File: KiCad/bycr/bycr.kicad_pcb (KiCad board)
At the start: 2 copper layers, 160.7 x 101.6 mm, 29 parts, among them J1 Conn_01x03, J2 Conn_01x03, J3 Conn_01x03, J4 Conn_01x03, J5 Conn_01x02, J6 Conn_01x02, SW1 SW_Push, U1 74HC595, U2 74HC595, U3 74HC165

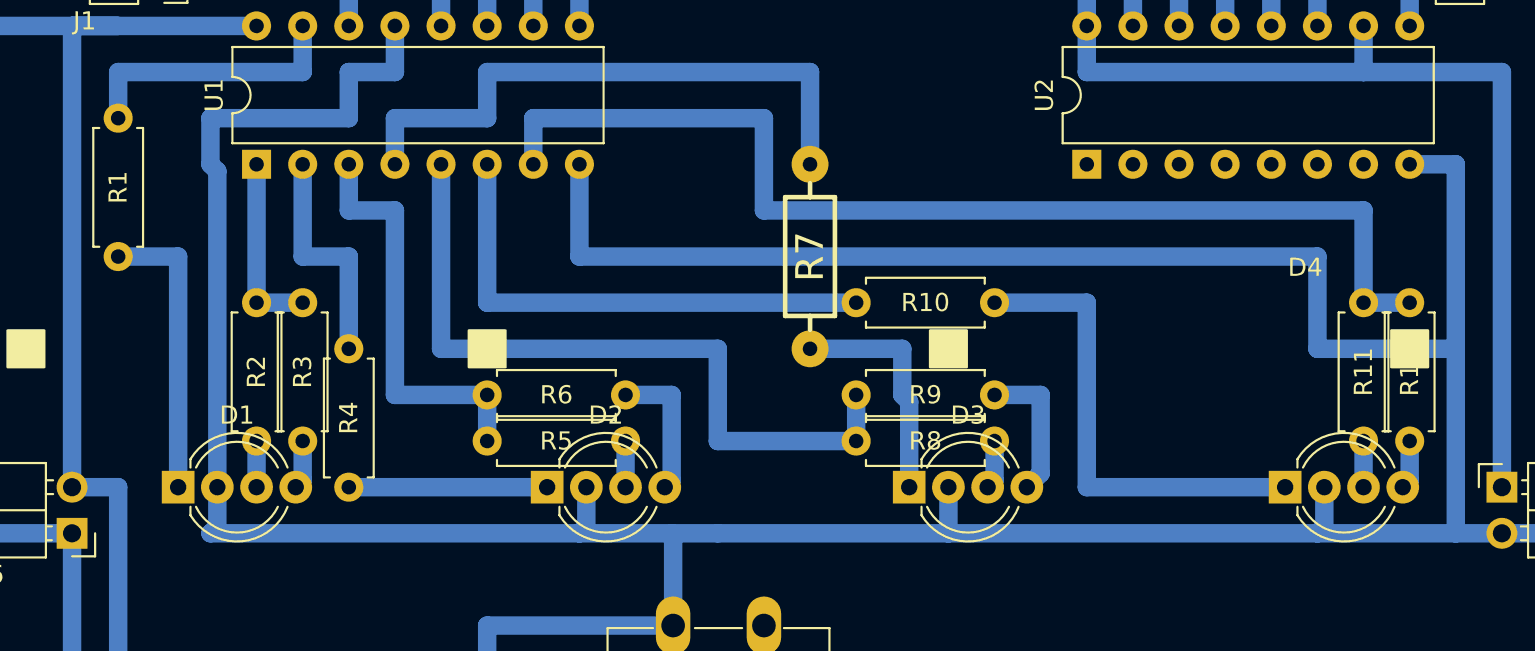
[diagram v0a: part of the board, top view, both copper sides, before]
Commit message: added custom rgbled footprint
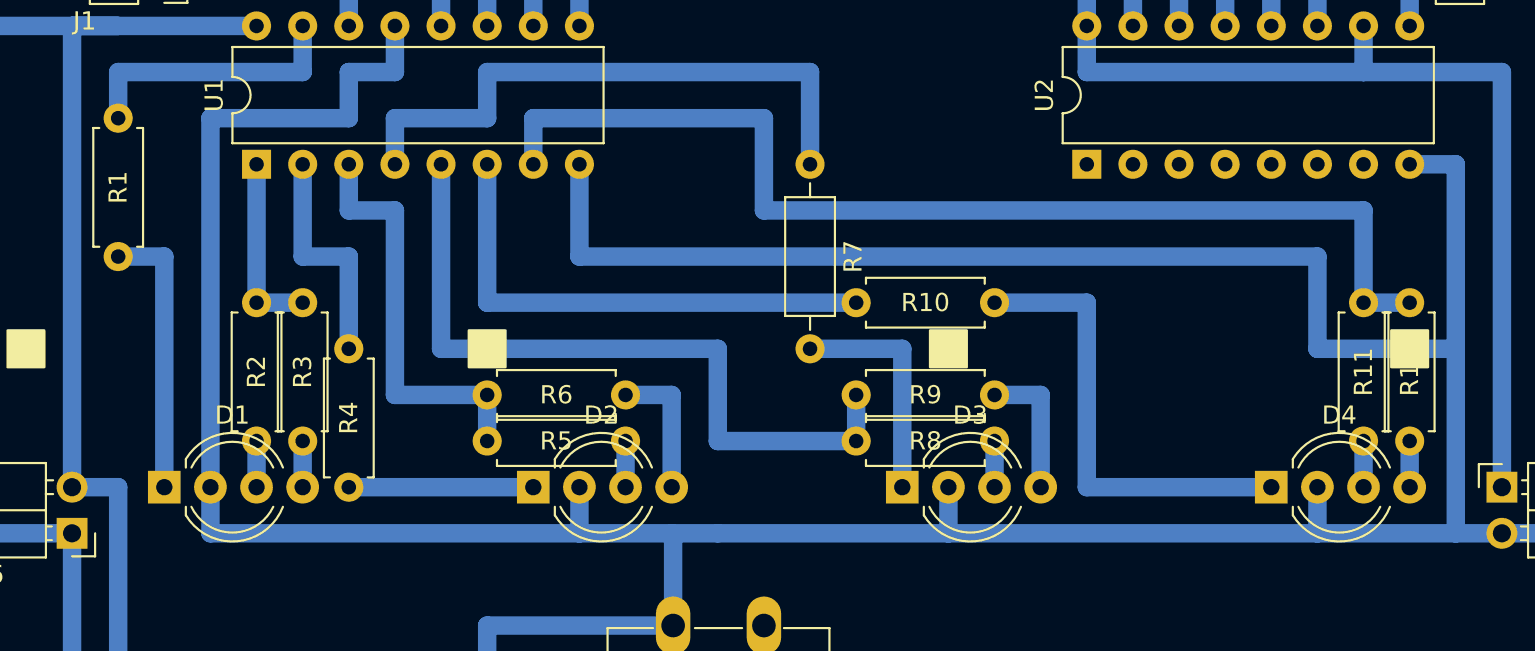
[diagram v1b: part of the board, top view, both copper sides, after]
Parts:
- D1, D2, D3, D4: footprint LED_THT:LED_D5.0mm-4_RGB_Wide_Pins -> Custom:LED_D5.0mm-4_RGB_Wide_Pins_Custom
- R7: footprint New_Library:Resistor -> Resistor_THT:R_Axial_DIN0207_L6.3mm_D2.5mm_P10.16mm_Horizontal
- moved D1 0.25 mm to (94.5, 81.3)
- moved D2 0.25 mm to (114.8, 81.3)
- moved D4 0.25 mm to (155.4, 81.3)
- moved D3 0.13 mm to (135.1, 81.3)
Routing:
- net Net-(D4-RA): track 26.2 -> 25.4 mm
- net Net-(D2-RA): track 10.9 -> 10.2 mm
- net Net-(D1-RA): track 16.0 -> 15.2 mm
- net GNDREF: track 458.3 -> 457.7 mm

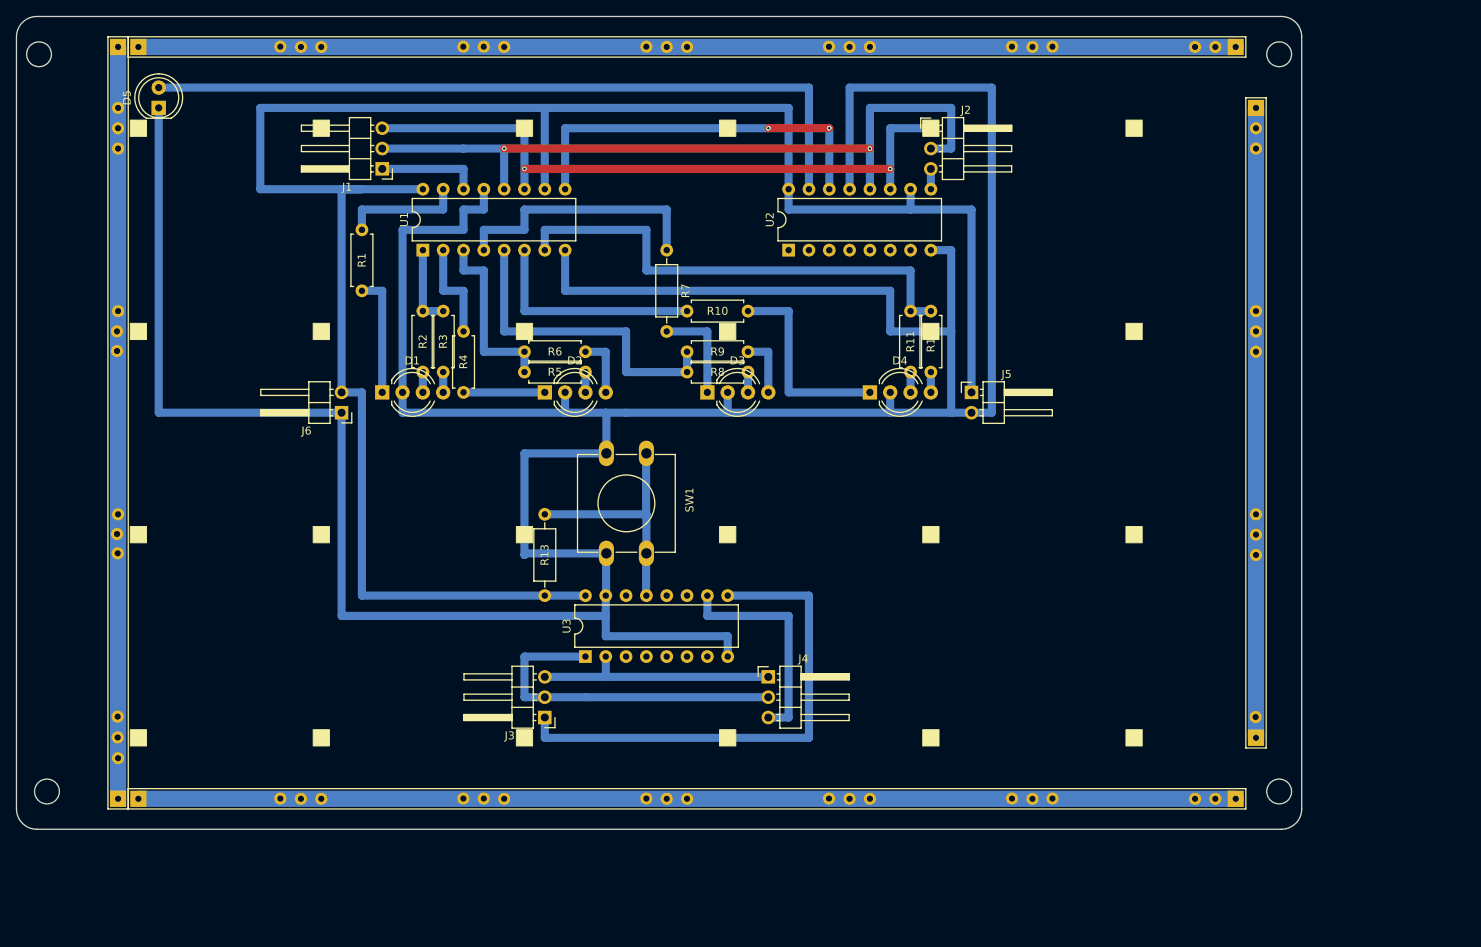
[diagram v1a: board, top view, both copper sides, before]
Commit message: rename bycr to bycr_hand
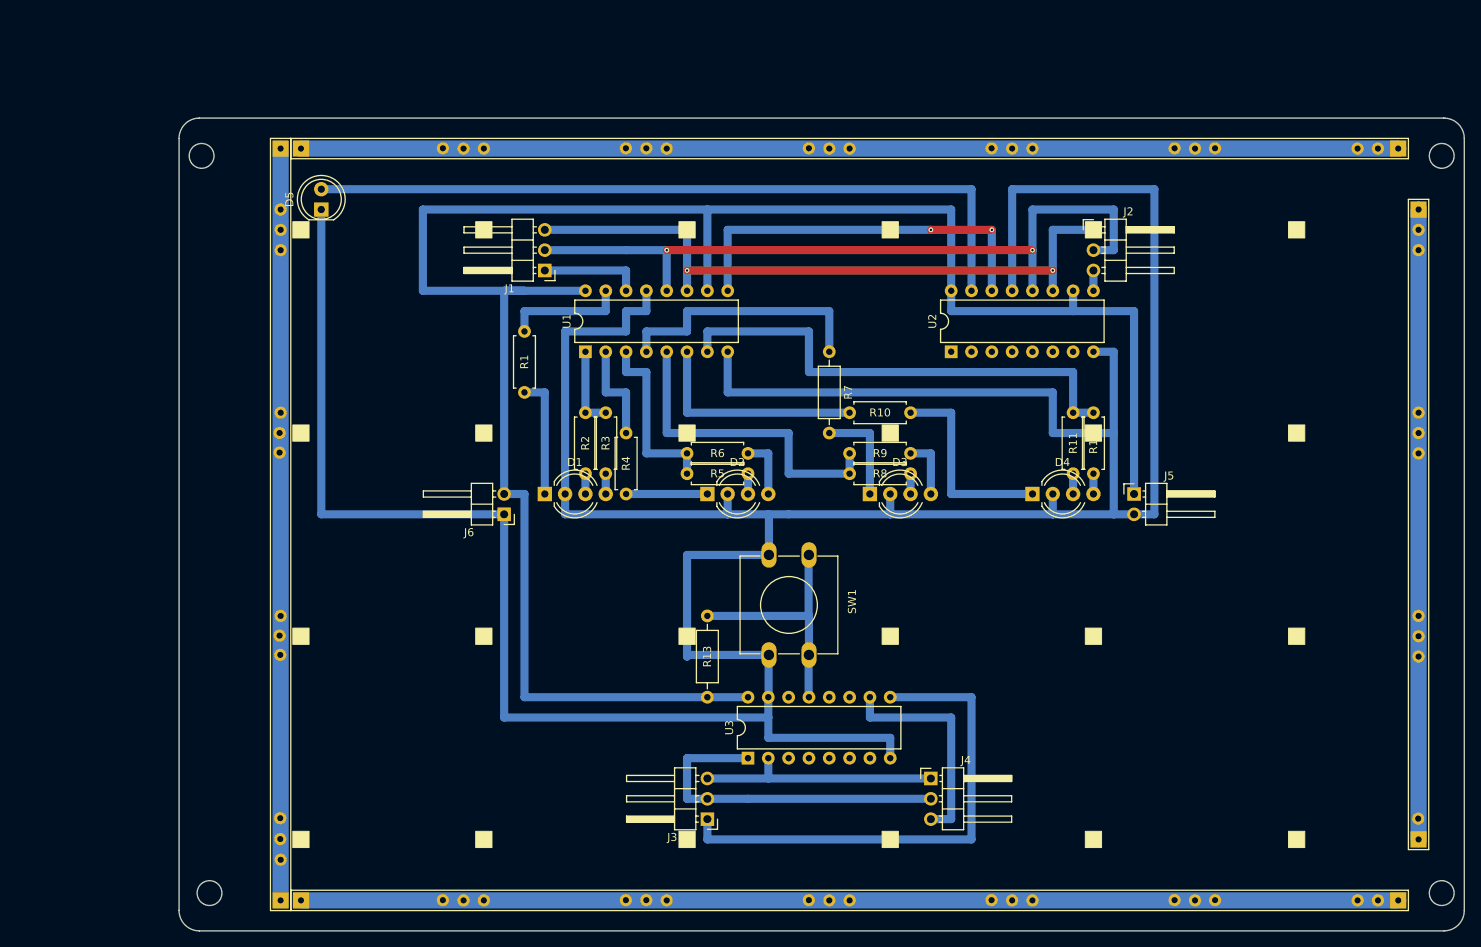
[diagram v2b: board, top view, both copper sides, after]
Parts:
- moved D3 24.0 mm to (155.4, 94.0)
- moved J5 24.0 mm to (188.0, 94.0)
- moved R7 24.0 mm to (149.9, 76.2)
- moved D1 24.0 mm to (114.8, 94.0)
- moved J3 24.0 mm to (134.6, 134.6)
- moved R1 24.0 mm to (111.8, 73.7)
- moved R5 24.0 mm to (132.1, 91.4)
- moved R6 24.0 mm to (132.1, 88.9)
- moved R13 24.0 mm to (134.6, 119.4)
- moved R3 24.0 mm to (121.9, 83.8)
- moved REF** 24.0 mm to (81.3, 50.8)
- moved D4 24.0 mm to (175.8, 94.0)
- moved D5 24.0 mm to (86.4, 58.4)
- moved J1 24.0 mm to (114.3, 66.0)
- moved J2 24.0 mm to (182.9, 61.0)
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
